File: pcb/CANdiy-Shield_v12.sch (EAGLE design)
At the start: 59 parts, among them IC2 MCP2551SO8, Q1 16MHz

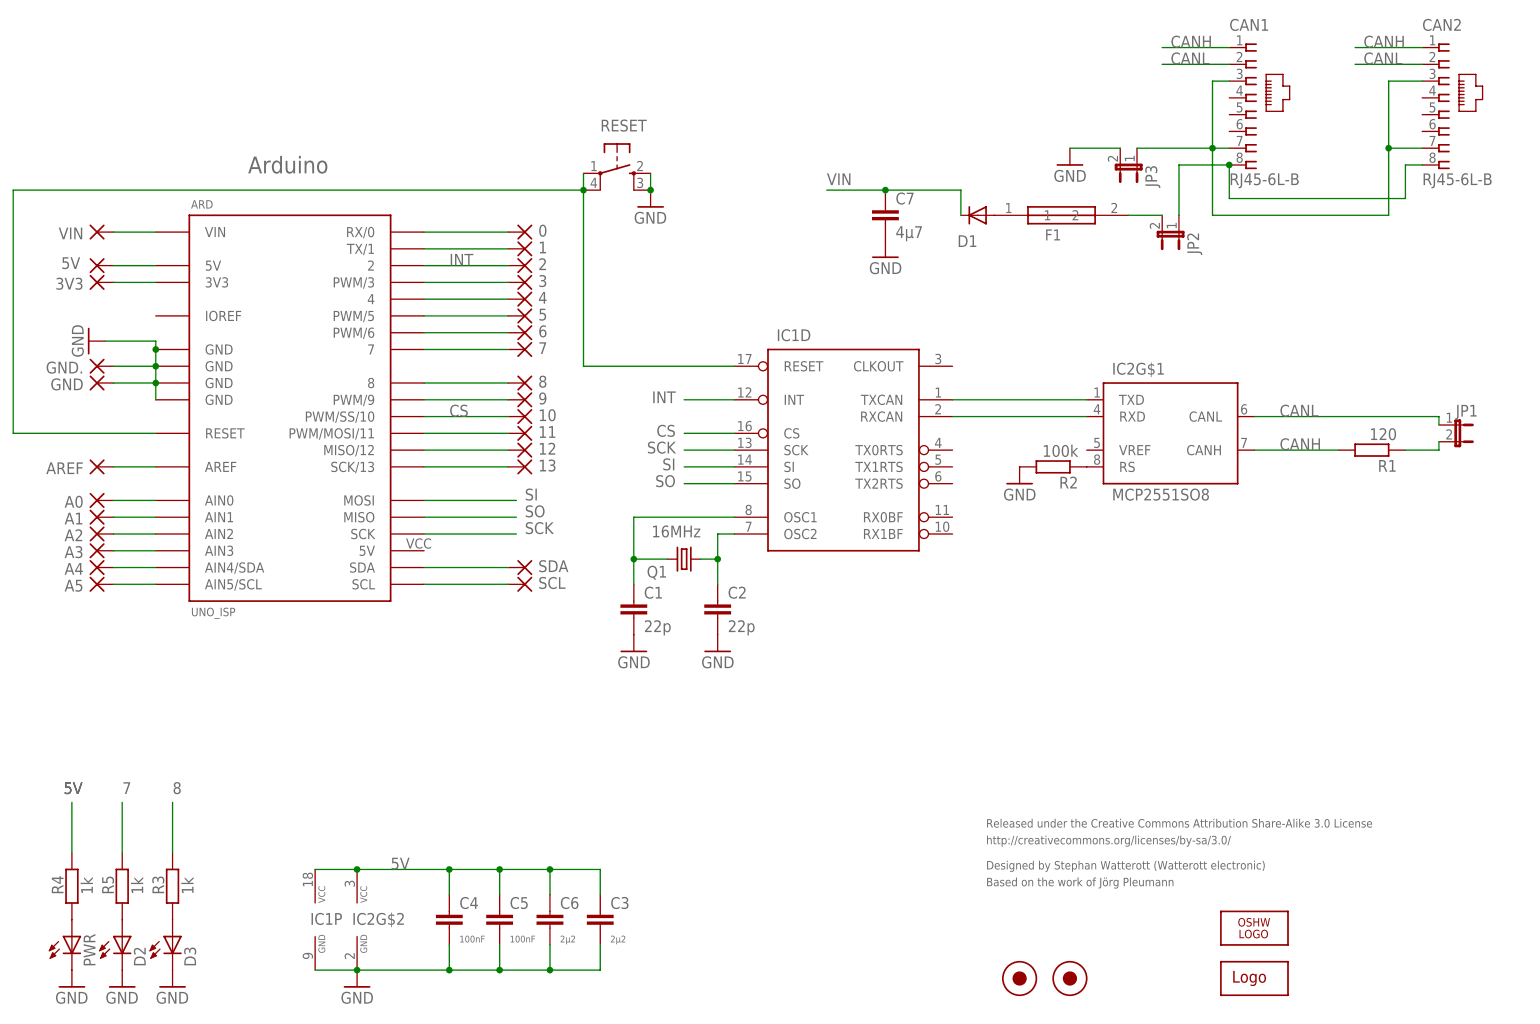
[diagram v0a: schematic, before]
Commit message: added jumper infos
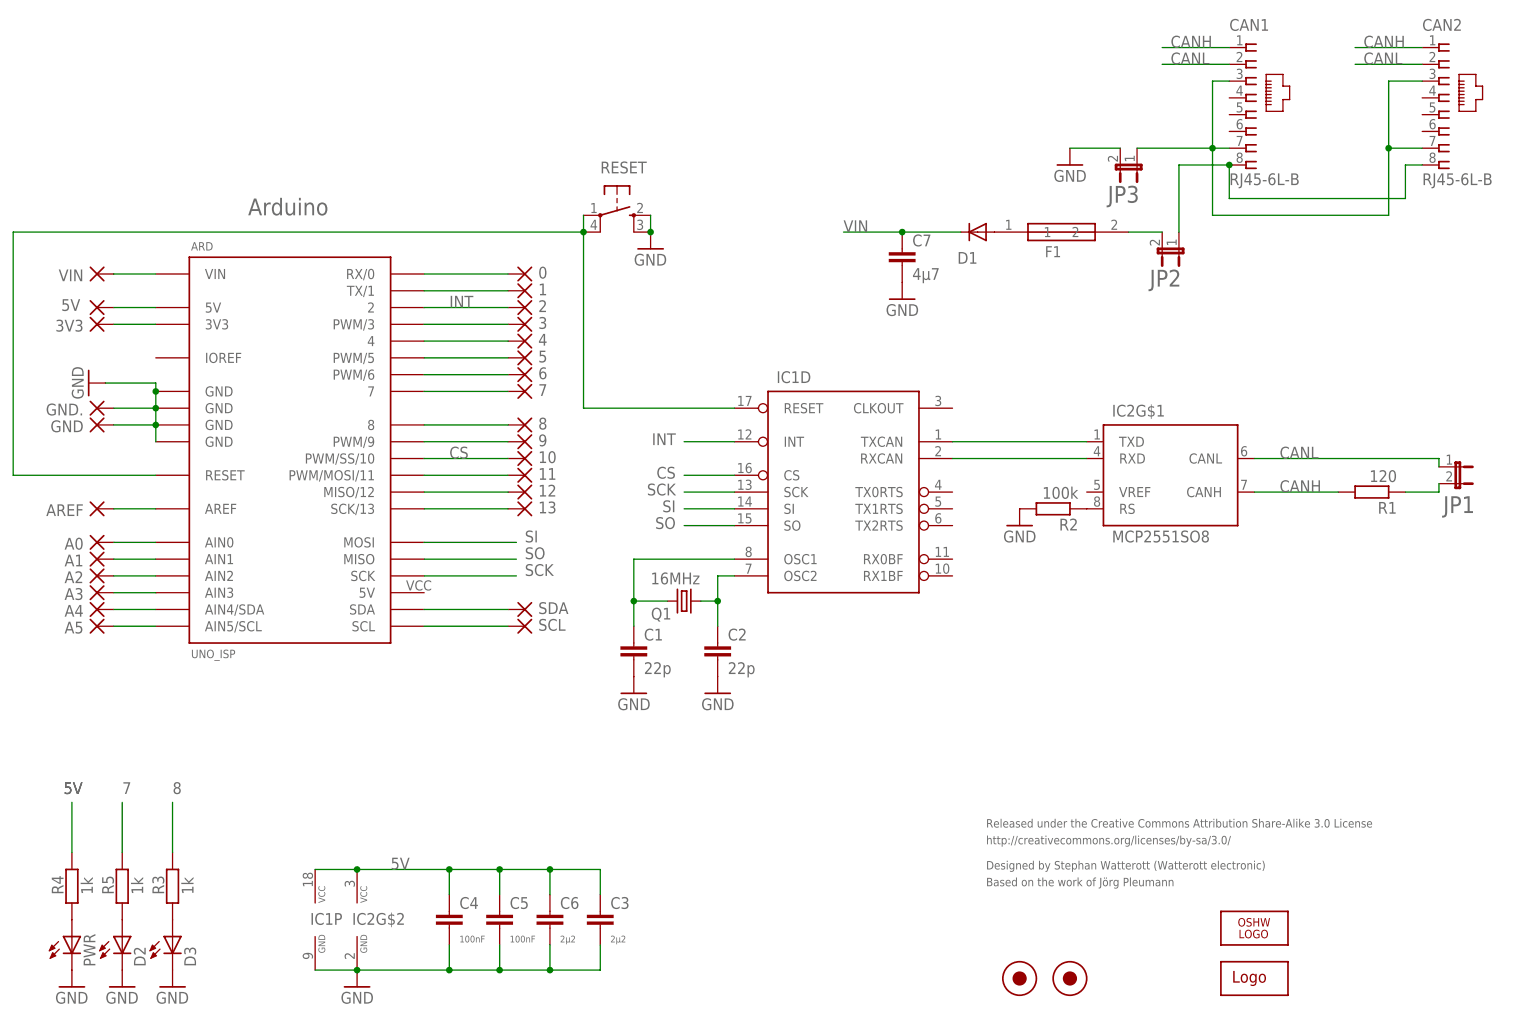
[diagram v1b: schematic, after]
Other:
- note added: "Short Jumpers JP2 and JP3 for power supply from RJ45 (required for Railuino)."
- moved on the sheet: 0, 1, 10, 11, 12, 13, 2, 3, 3V3, 4, 5, 6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

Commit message: updated schematics and layout files
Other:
- note added: "Released under the Creative Commons Attribution Share-Alike License"
- note added: "http://creativecommons.org/licenses/by-sa/4.0/"
- note removed: "Released under the Creative Commons Attribution Share-Alike 3.0 License"
- note removed: "http://creativecommons.org/licenses/by-sa/3.0/"
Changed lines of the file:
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@@
 <?xml version="1.0" encoding="utf-8"?>
 <!DOCTYPE eagle SYSTEM "eagle.dtd">
-<eagle version="6.4">
+<eagle version="6.5.0">
 <drawing>
 <settings>
@@
 <setting verticaltext="up"/>
 </settings>
-<grid distance="0.05" unitdist="inch" unit="inch" style="lines" multiple="1" display="yes" altdistance="0.025" altunitdist="inch" altunit="inch"/>
+<grid distance="0.1" unitdist="inch" unit="inch" style="lines" multiple="1" display="no" altdistance="0.01" altunitdist="inch" altunit="inch"/>
 <layers>
 <layer number="1" name="Top" color="4" fill="1" visible="no" active="no"/>
@@
 <sheet>
 <plain>
-<text x="161.29" y="34.29" size="1.27" layer="95">Released under the Creative Commons Attribution Share-Alike 3.0 License</text>
-<text x="161.29" y="31.75" size="1.27" layer="95">http://creativecommons.org/licenses/by-sa/3.0/</text>
+<text x="161.29" y="34.29" size="1.27" layer="95">Released under the Creative Commons Attribution Share-Alike License</text>
+<text x="161.29" y="31.75" size="1.27" layer="95">http://creativecommons.org/licenses/by-sa/4.0/</text>
 <text x="161.29" y="27.94" size="1.27" layer="95">Designed by Stephan Watterott (Watterott electronic)</text>
 <text x="49.53" y="127" size="2.54" layer="95">Arduino</text>
